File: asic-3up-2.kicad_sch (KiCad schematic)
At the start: 66 parts, among them J16 Conn_01x01, J17 Conn_01x01, J8 Conn_01x01, J9 Conn_01x01, U57 MCP1824T-1202E/OT, U58 MCP1824T-1202E/OT, U59 MCP1824T-1202E/OT, U60 MCP1824T-0802E, U61 MCP1824T-0802E, U62 MCP1824T-0802E, U63 BM1362AC_MODE1, U64 BM1362AC_MODE0, U65 BM1362AC_MODE1

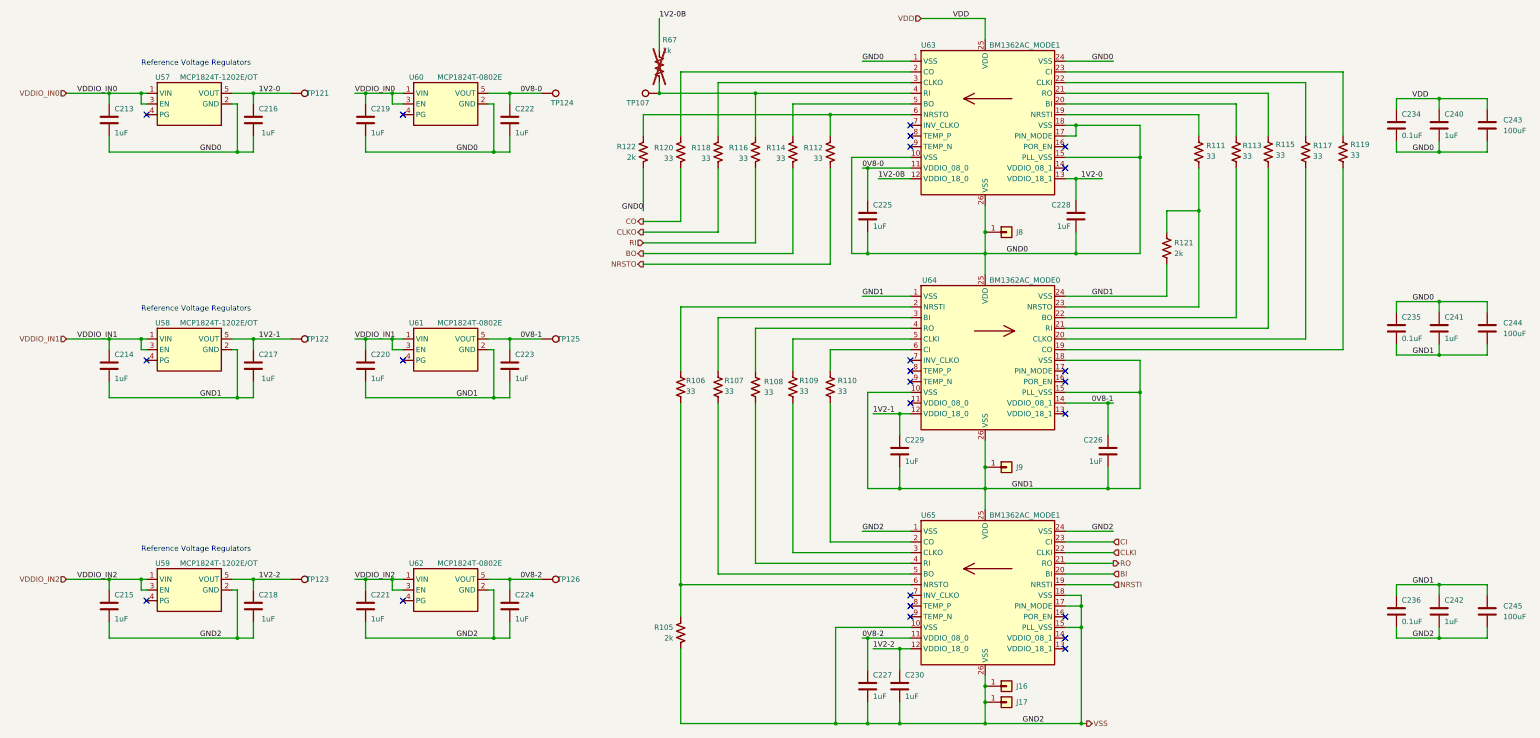
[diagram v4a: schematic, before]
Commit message: Added Mfg to BOM
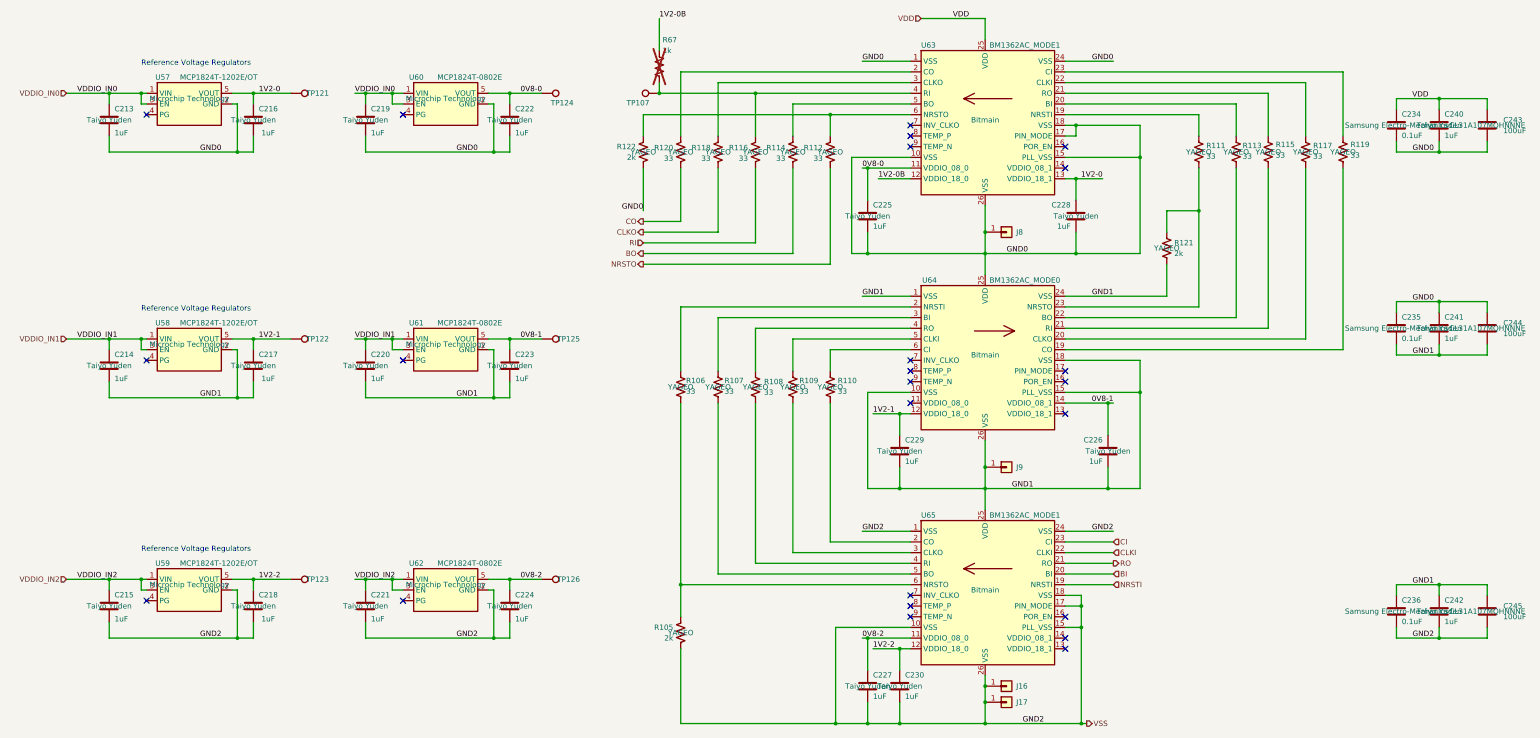
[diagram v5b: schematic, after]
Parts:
- C213, C214, C215, C216, C217, C218, C219, C220, C221, C222, C223, C224, C225, C226, C227, C228, C229, C230, C240, C241, C242: Manufacturer (none) -> Taiyo Yuden
- C234, C235, C236: Manufacturer (none) -> Samsung Electro-Mechanics
- C243, C244, C245: Manufacturer (none) -> CL31A107MQHNNNE
- R105, R106, R107, R108, R109, R110, R111, R112, R113, R114, R115, R116, R117, R118, R119, R120, R121, R122: Manufacturer (none) -> YAGEO
- U57, U58, U59, U60, U61, U62: Manufacturer (none) -> Microchip Technology
- U63, U64, U65: Manufacturer (none) -> Bitmain

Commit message: missed a few
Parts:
- U63, U64, U65: PARTNO (none) -> BM1362AC
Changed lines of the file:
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@@
+			)
+		)
+		(property "PARTNO" "BM1362AC"
+			(at 248.92 71.12 0)
+			(effects
+				(font
+					(size 1.27 1.27)
+				)
 			)
 		)
@@
 			)
 		)
+		(property "PARTNO" "BM1362AC"
+			(at 248.92 127 0)
+			(effects
+				(font
+					(size 1.27 1.27)
+				)
+			)
+		)
 		(pin "10"
 		)
@@
 			(at 248.92 182.88 0)
 			(effects
+				(font
+					(size 1.27 1.27)
+				)
+			)
+		)
+		(property "PARTNO" "BM1362AC"
+			(at 248.92 182.88 0)
+			(effects

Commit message: Revert "Merge commit '7c9b4c648e8c0cd5eb9ee29b12963992edc9d4fe' into v4"
This reverts commit 16575a5f433ae2a288f6a827ad209afb5e5f3437, reversing
changes made to e5a5abad8ce065f31a2bf126cd7235584780cb09.
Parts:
- removed J16: Conn_01x01, emberone:14x9_powertab_L, symbol Connector_Generic:Conn_01x01
- removed J17: Conn_01x01, emberone:14x9_powertab_R, symbol Connector_Generic:Conn_01x01
- C213, C214, C215, C216, C217, C218, C219, C220, C221, C222, C223, C224, C225, C226, C227, C228, C229, C230, C240, C241, C242: Manufacturer Taiyo Yuden -> (none)
- C234, C235, C236: DK 1276-1234-1-ND -> 478-KGM05AR71C104KHCT-ND; Manufacturer Samsung Electro-Mechanics -> (none); PARTNO CL05A104KO5NNNC -> KGM05AR71C104KH
- C243, C244, C245: Manufacturer CL31A107MQHNNNE -> (none)
- J8, J9: now in the parts list
- R105, R106, R107, R108, R109, R110, R111, R112, R113, R114, R115, R116, R117, R118, R119, R120, R121, R122: Manufacturer YAGEO -> (none)
- R67: now left out of the parts list
- U57, U58, U59: ALT1 (none) -> LDK120M12R; Manufacturer Microchip Technology -> (none)
- U60, U61, U62: ALT1 (none) -> LDK120M08R; Manufacturer Microchip Technology -> (none)
- U63, U64, U65: Manufacturer Bitmain -> (none); PARTNO BM1362AC -> (none)

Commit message: added some LCSC parts numbers and regenerated BOM
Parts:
- C213, C214, C215, C216, C217, C218, C219, C220, C221, C222, C223, C224, C225, C226, C227, C228, C229, C230, C240, C241, C242: LCSC (none) -> C52923
- C234, C235, C236: LCSC (none) -> C307331
- C243, C244, C245: LCSC (none) -> C15008
- R105, R121, R122: LCSC (none) -> C60488
- R106, R107, R108, R109, R110, R111, R112, R113, R114, R115, R116, R117, R118, R119, R120: LCSC (none) -> C25105
